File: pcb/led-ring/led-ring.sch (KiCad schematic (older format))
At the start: 30 parts

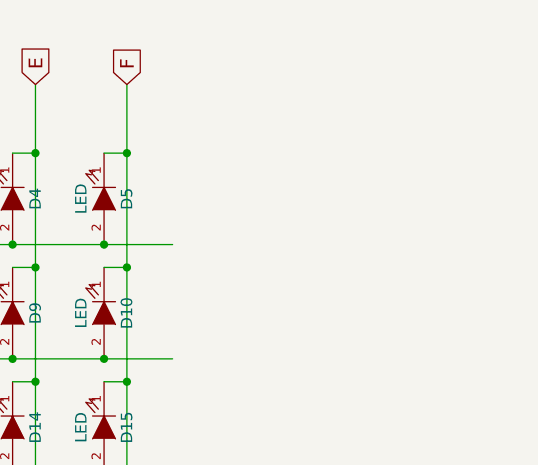
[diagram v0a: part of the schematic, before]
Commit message: o Add flat-flex footprint.
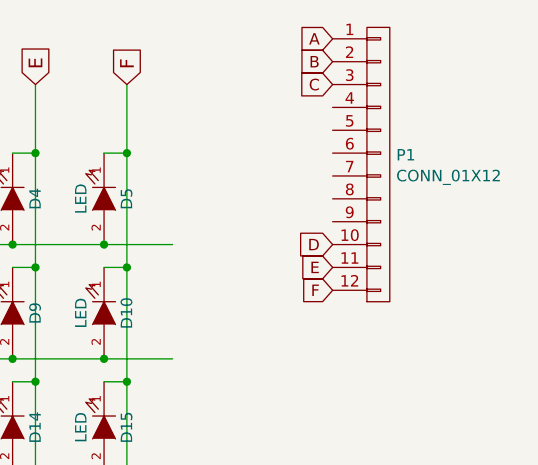
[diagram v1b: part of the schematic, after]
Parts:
- added P1: CONN_01X12, knopf:FlatFlex, symbol CONN_01X12
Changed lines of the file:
@@
 LIBS:contrib
 LIBS:valves
+LIBS:led-ring-cache
 EELAYER 25 0
 EELAYER END
@@
 Text GLabel 4700 2450 1    60   Input ~ 0
 F
+$Comp
+L CONN_01X12 P1
+U 1 1 57F9B599
+P 5800 2800
+F 0 "P1" H 5878 2841 50  0000 L CNN
+F 1 "CONN_01X12" H 5878 2750 50  0000 L CNN
+F 2 "knopf:FlatFlex" H 5800 2800 50  0001 C CNN
+F 3 "" H 5800 2800 50  0000 C CNN
+	1    5800 2800
+	1    0    0    -1
+$EndComp
+Text GLabel 5600 2250 0    50   Input ~ 0
+A
+Text GLabel 5600 2350 0    50   Input ~ 0
+B
+Text GLabel 5600 2450 0    50   Input ~ 0
+C
+Text GLabel 5600 3150 0    50   Input ~ 0
+D
+Text GLabel 5600 3250 0    50   Input ~ 0
+E
+Text GLabel 5600 3350 0    50   Input ~ 0
+F
 $EndSCHEMATC

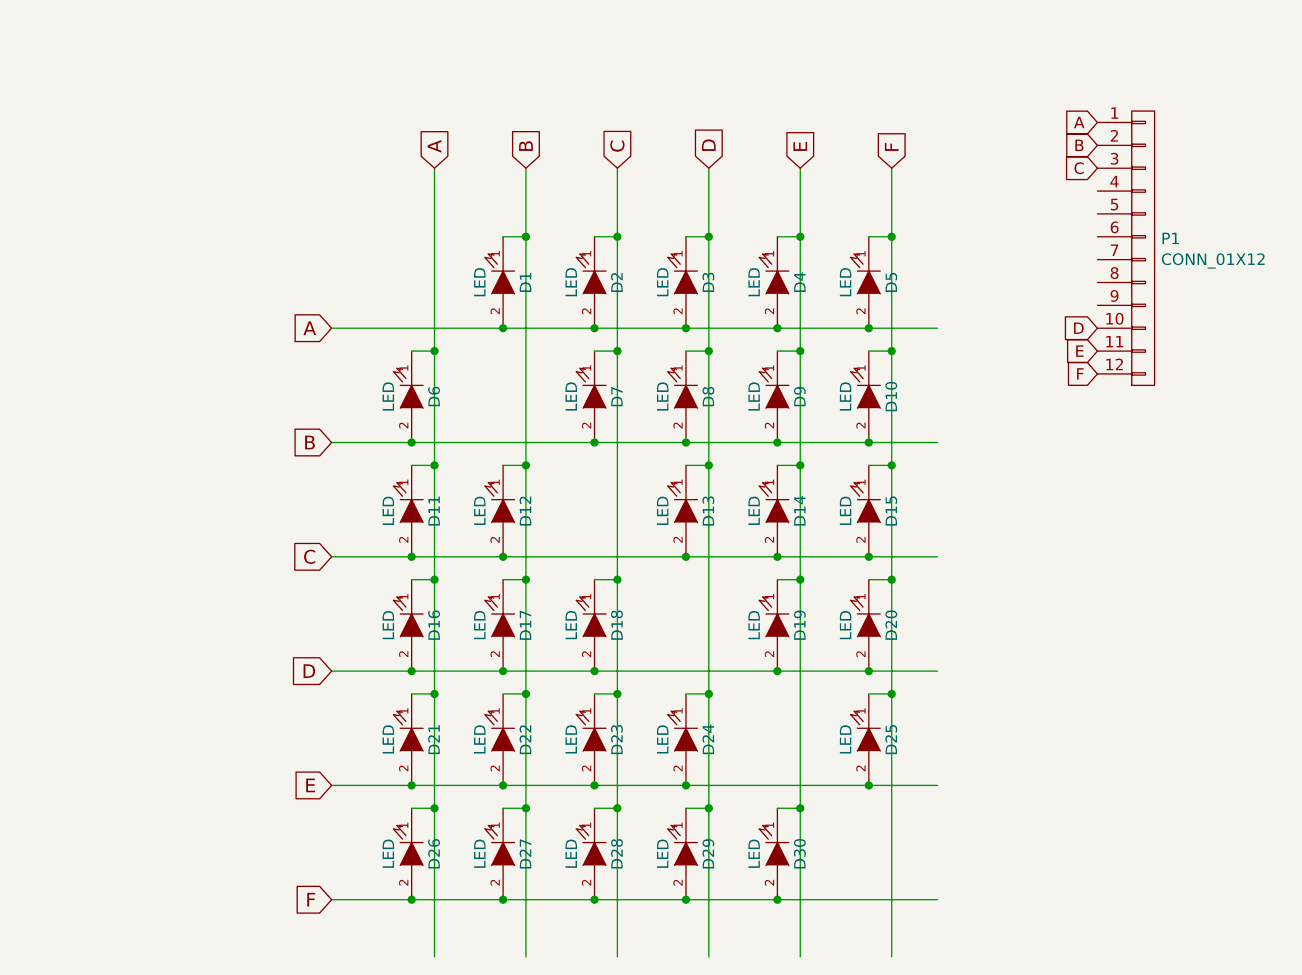
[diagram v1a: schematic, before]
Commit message: o Add IR receiver. o Shape ring in a way so that receiver fits.
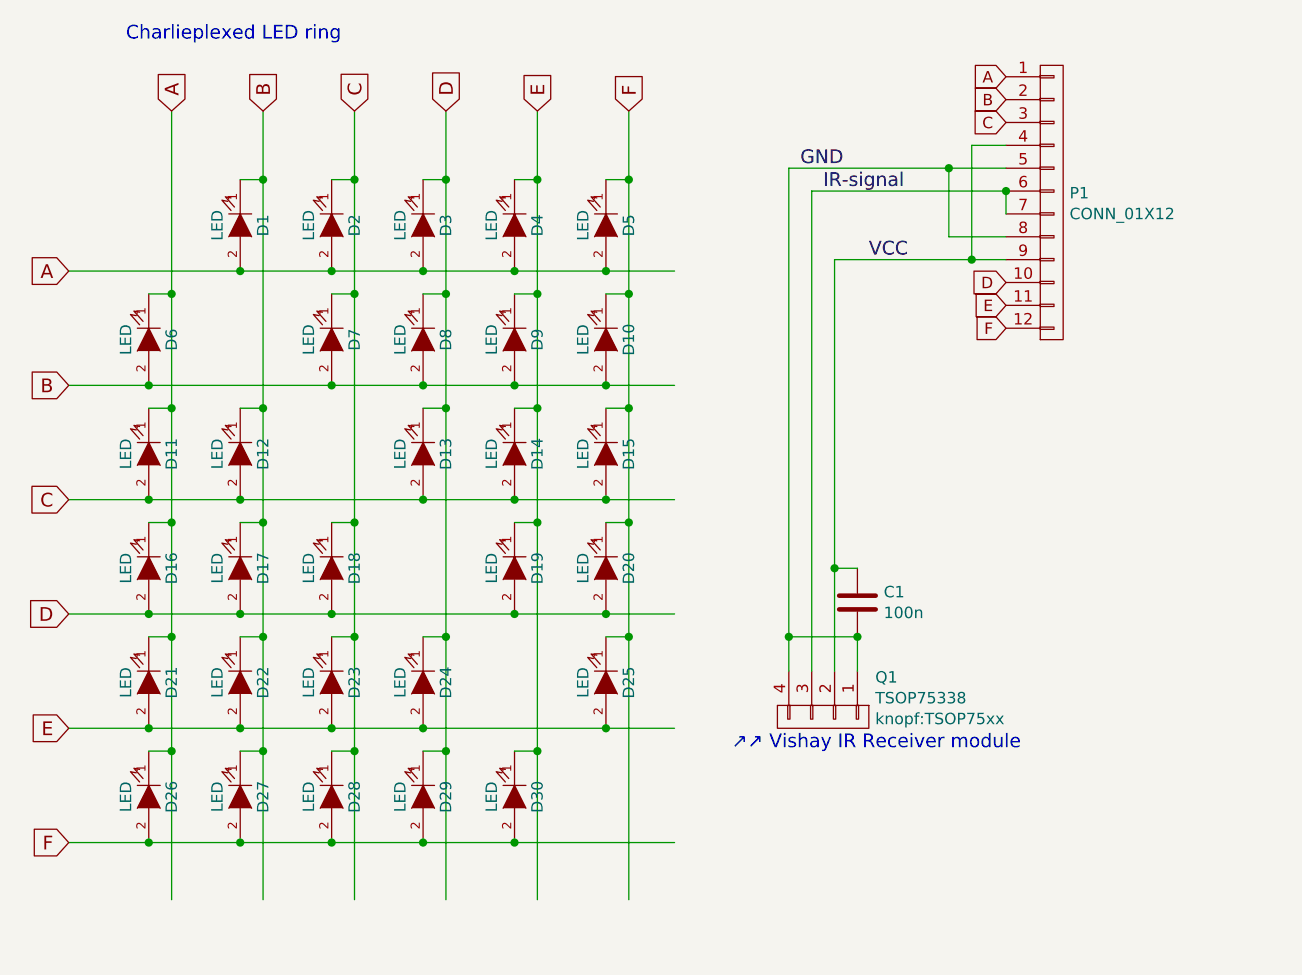
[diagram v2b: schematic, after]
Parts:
- added C1: 100n, Capacitors_SMD:C_0603, symbol C
- added Q1: TSOP75338, knopf:TSOP75xx, symbol CONN_01X04
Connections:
- net labels added: GND, IR-signal, VCC
- wire segments 42 -> 56
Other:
- note added: "Charlieplexed LED ring"
- note added: "↗↗ Vishay IR Receiver module"
- moved on the sheet: D1, D10, D11, D12, D13, D14, D15, D16, D17, D18, D19, D2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
